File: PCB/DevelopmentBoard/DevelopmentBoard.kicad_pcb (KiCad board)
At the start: 2 copper layers, 128.3 x 64.8 mm, 37 parts, among them IC1 FE1.1S_USB_Controller, J1 Conn_01x04_MountingPin, J2 USB-A, J3 USB-A, J4 CRJ007_RJ45, U1 Pi_CM4, U2 Barometer_Grove, U3 D24V22F5, U4 Micro-USB, U5 VN-100_Breakout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

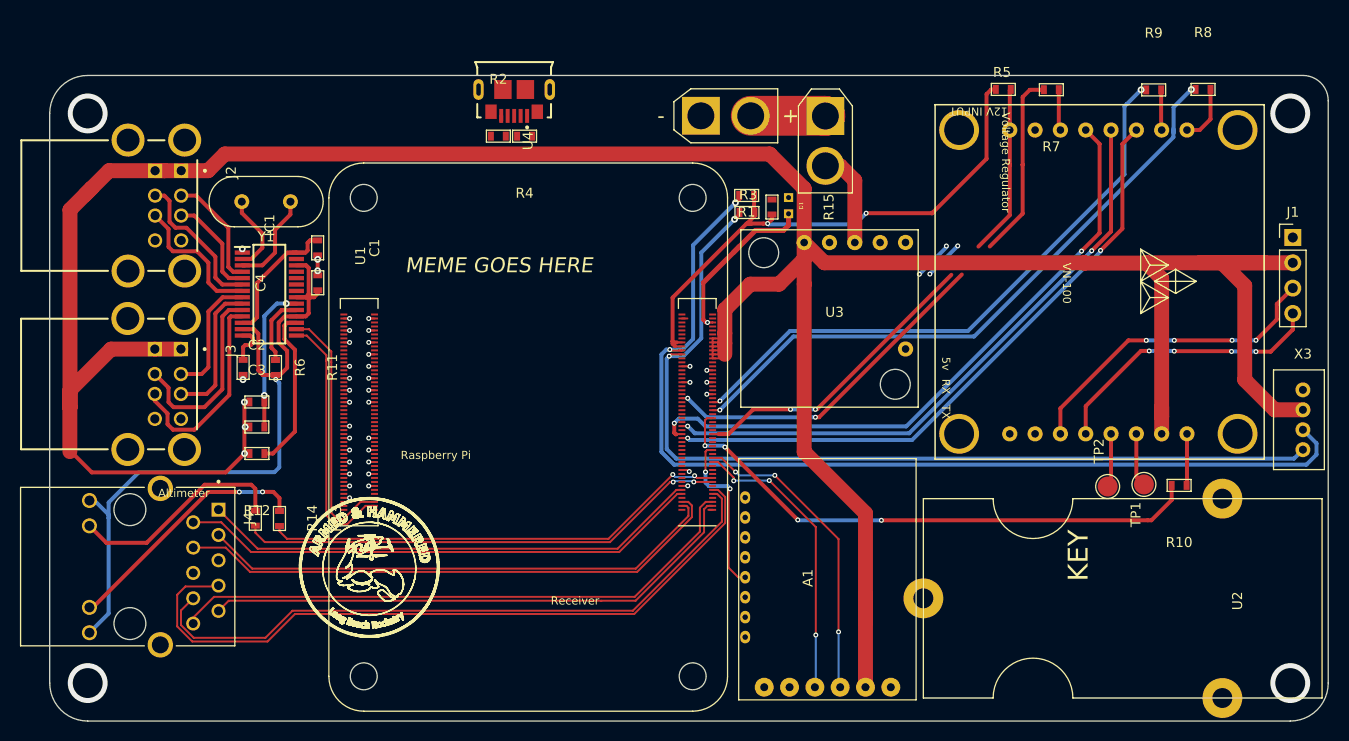
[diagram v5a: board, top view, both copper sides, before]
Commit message: Eliminated perpendicular trace routing
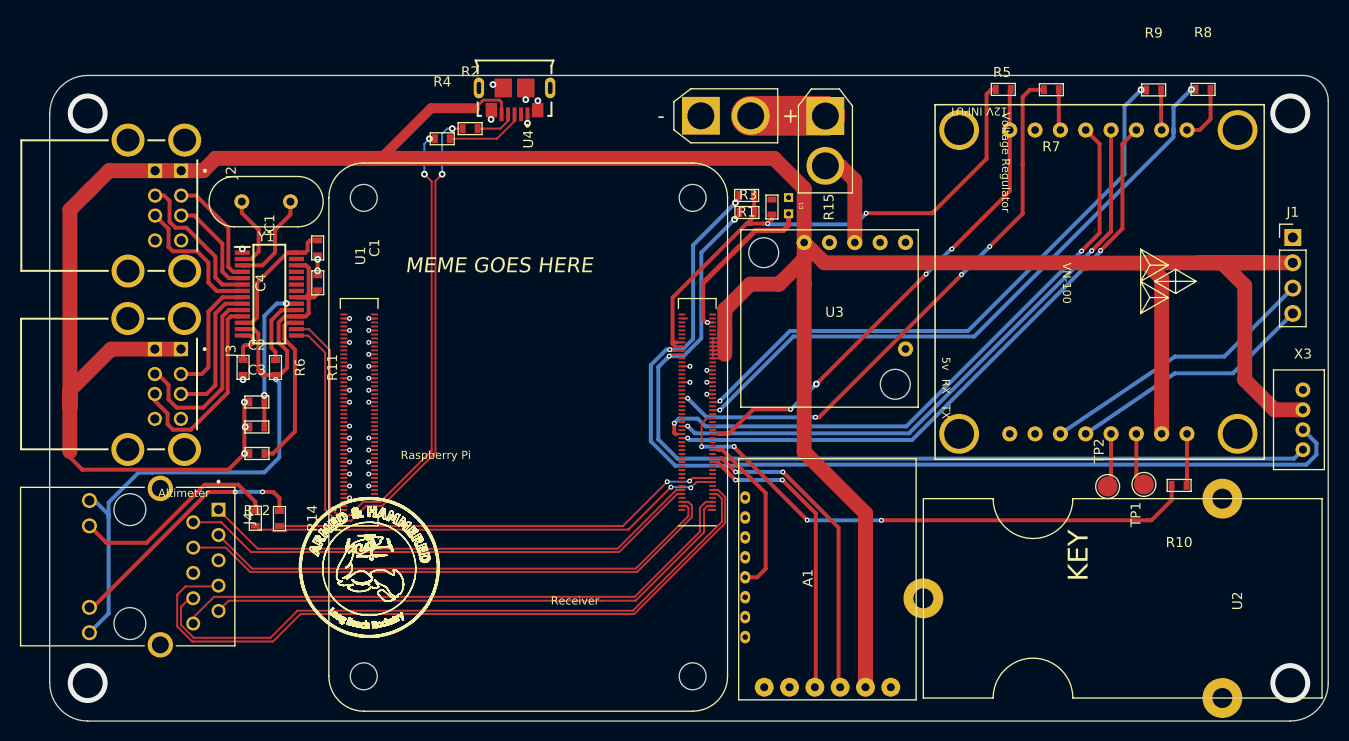
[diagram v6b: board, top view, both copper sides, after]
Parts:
- moved R4 8.26 mm to (131.8, 72.1), turned to 0 degrees
- moved R2 2.93 mm to (134.6, 71.1)
- moved U4 0.16 mm to (140.4, 69.7)
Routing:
- net /D0-: track 25.9 -> 68.5 mm, vias 0 -> 2
- net /D0+: track 26.0 -> 65.8 mm, vias 0 -> 2
- net +5V: track 320.5 -> 336.4 mm
- net Net-(R4-Pad2): track 0.00 -> 7.92 mm
- net Net-(R2-Pad2): track 0.00 -> 4.14 mm
- net GND: track 24.2 -> 28.0 mm, vias 38 -> 41
- net Net-(J1-Pad3): track 31.8 -> 28.5 mm, vias 4 -> 0
- net Net-(J1-Pad4): track 28.4 -> 25.2 mm, vias 4 -> 0
- net /ETH_LEDG: track 47.2 -> 45.5 mm
- net /VN-100_CS: track 51.7 -> 50.3 mm
- net /ETH_LEDY: track 49.5 -> 48.3 mm
- net /SDA: track 100.9 -> 101.9 mm
- net /CH1: track 30.9 -> 31.8 mm, vias 3 -> 2
- net Net-(J4-Pad12): track 22.1 -> 21.4 mm
- net /CH2: track 29.4 -> 30.1 mm, vias 3 -> 2
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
